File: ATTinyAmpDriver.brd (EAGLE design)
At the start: 30 x 15 mm, 22 parts, among them Q1 BSP100, U1 SPX5205M5-L-3-3, U2 ATTINY5-TSHR, U3 MCP6001, X1 DIODES, X2 INPUT

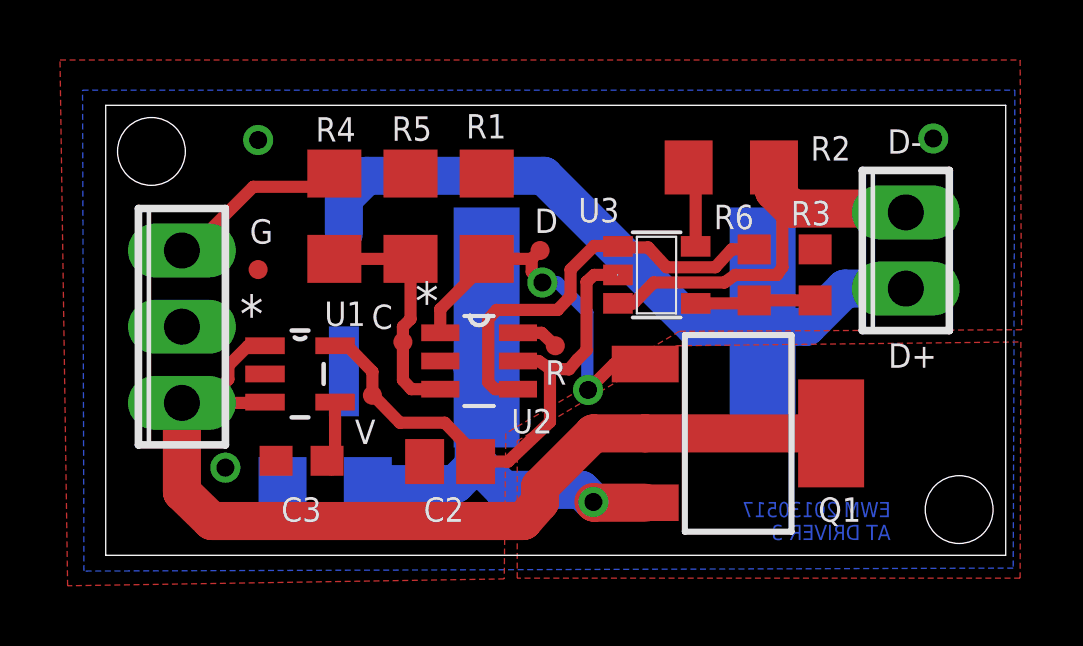
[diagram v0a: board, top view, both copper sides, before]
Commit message: P Channel MOSFET
Changed from Incorrect N-Channel to P-Channel High side switch on the
Driver Circuit.
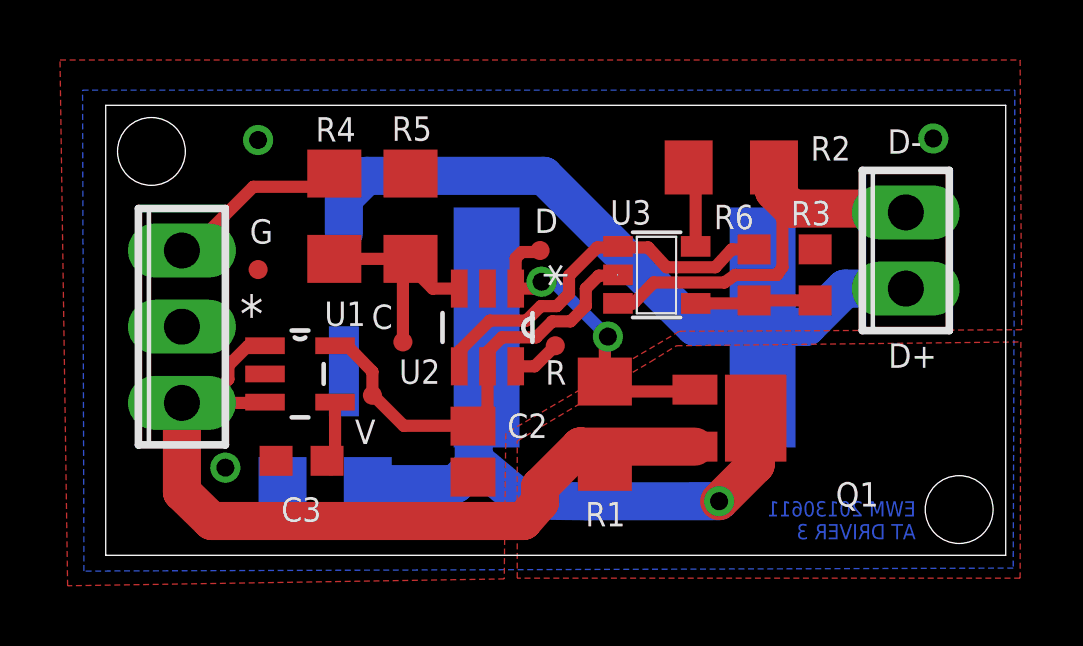
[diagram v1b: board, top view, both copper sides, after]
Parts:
- Q1: value BSP100 -> SI2301CDS; device Personal:SOT223 -> Combined:SOT-23_POWER
- moved R1 7.97 mm to (16.6, 4.37), turned to 90 degrees
- moved U2 1.15 mm to (12.7, 7.59), turned to 270 degrees
- moved C2 0.83 mm to (12.2, 3.45), turned to 270 degrees
- moved Q1 0.77 mm to (21.7, 4.57)
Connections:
- net +14V: now also Q1.P$2, R1.1; no longer Q1.2, Q1.TAB
- net GND: no longer R1.1
- net L+: now also Q1.P$3; no longer Q1.3
- net MOSFET: now also Q1.P$1; no longer Q1.1
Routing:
- net L+: track 15.2 -> 20.8 mm
- net +14V: track 32.4 -> 27.7 mm
- net VCC: track 17.7 -> 14.6 mm
- net MOSFET: track 12.7 -> 10.6 mm
- net MEASURE: track 14.2 -> 12.7 mm
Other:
- board text added: "EWM 20130611 AT DRIVER 3"
- board text removed: "EWM 20130517 AT DRIVER 3"

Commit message: Added Driving transistor for P-FET
Added driver transistor to P Channel MOSFET and capacitor to op-amp
output.
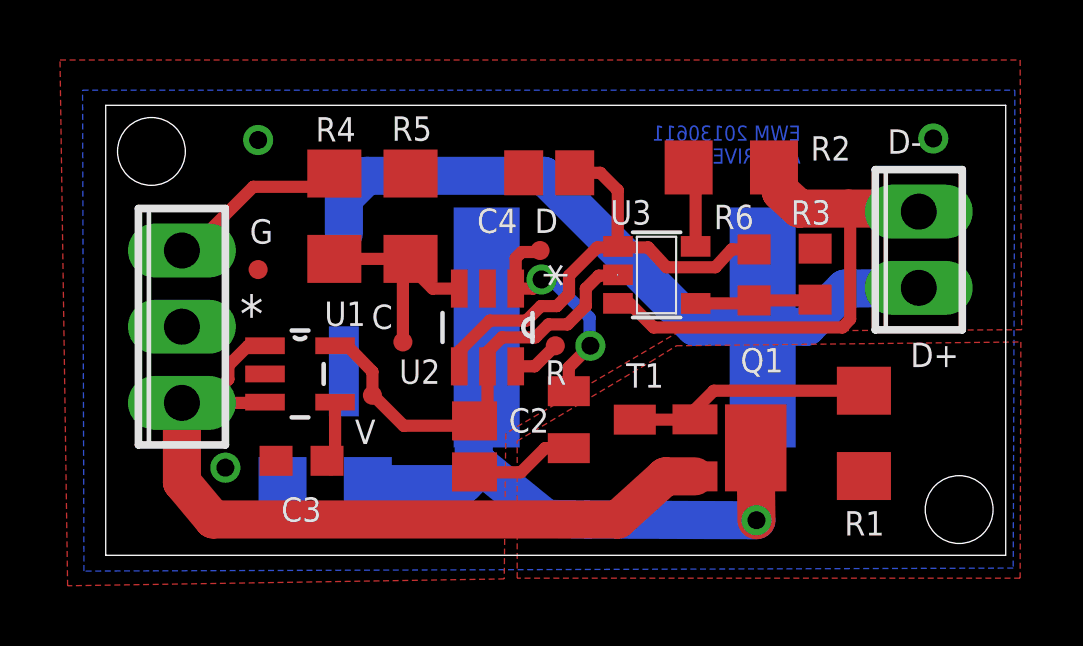
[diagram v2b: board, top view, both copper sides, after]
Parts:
- added C4: .1u, resistor:C0805
- added T1: BC846, transistor-neu-to92:SOT23
- moved R1 8.64 mm to (25.3, 4.06)
- moved Q1 0.99 mm to (21.7, 3.58)
- moved X1 0.43 mm to (27.1, 10.2)
- moved C2 0.18 mm to (12.3, 3.63)
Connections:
- new net N$5: Q1.P$1, R1.2, T1.3
- net GND: now also C4.2, T1.2
- net MEASURE: now also C4.1
- net MOSFET: now also T1.1; no longer Q1.P$1, R1.2
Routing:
- net N$5: track 0.00 -> 8.23 mm
- net MEASURE: track 12.7 -> 16.3 mm
- net GND: track 2.73 -> 6.21 mm
- net MOSFET: track 10.6 -> 7.83 mm
- net D-: track 14.9 -> 17.6 mm
- net +14V: track 27.7 -> 26.7 mm
- net L+: track 20.8 -> 21.5 mm

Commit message: Removed LED filter circuit
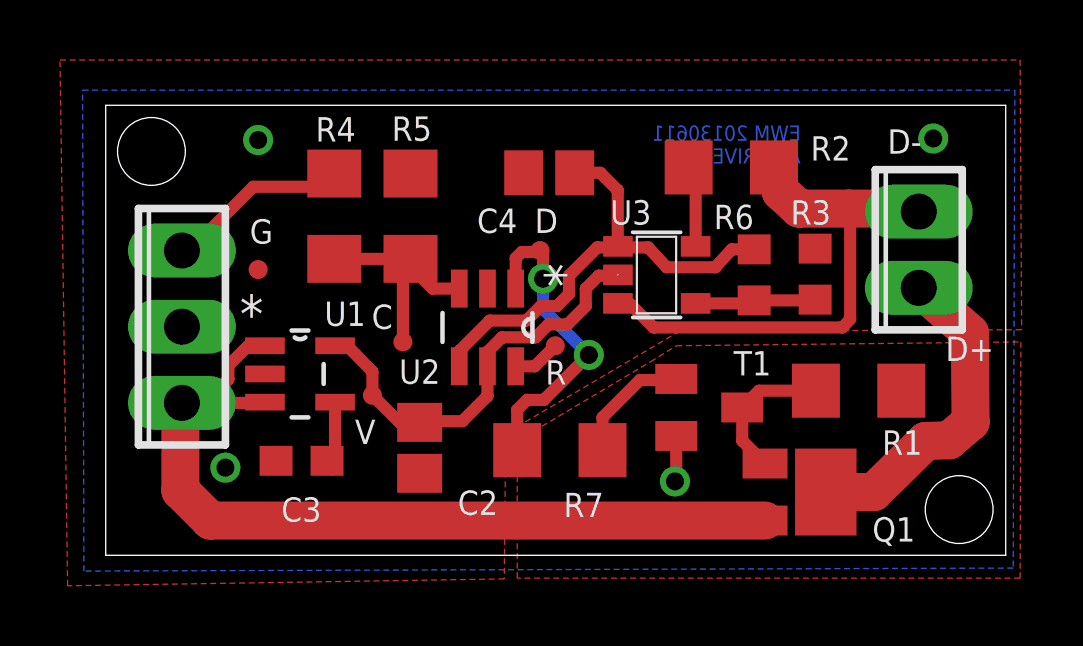
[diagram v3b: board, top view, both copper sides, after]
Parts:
- removed C1: 100u, Personal:CDE-AVE-X
- removed D1: CD1206-B260, Personal:D1206
- removed L1: SRN8040, Personal:SRN8040
- added R7: 10k, resistor:R1206
- R1: value 10k -> 1k
- moved T1 3.60 mm to (20.1, 4.93)
- moved Q1 2.76 mm to (24.0, 2.11)
- moved C2 1.83 mm to (10.5, 3.58)
- moved R1 1.43 mm to (25.1, 5.49), turned to 180 degrees
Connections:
- removed net L+: D1.1, L1.P$1, Q1.P$3
- new net N$6: R7.2, T1.1
- net GND: no longer C1.C-, D1.2
- net MOSFET: now also R7.1; no longer T1.1
- net N$3: now also Q1.P$3; no longer C1.C+, L1.P$2
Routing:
- net L+: track 21.5 -> 0.00 mm, vias 1 -> 0
- net N$3: track 23.3 -> 11.0 mm
- net N$6: track 0.00 -> 4.08 mm
- net N$5: track 8.23 -> 4.87 mm
- net MOSFET: track 7.83 -> 10.6 mm
- net +14V: track 26.7 -> 28.7 mm
- net GND: track 6.21 -> 4.27 mm, vias 3 -> 4

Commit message: Removed Cap from OpAmp Output
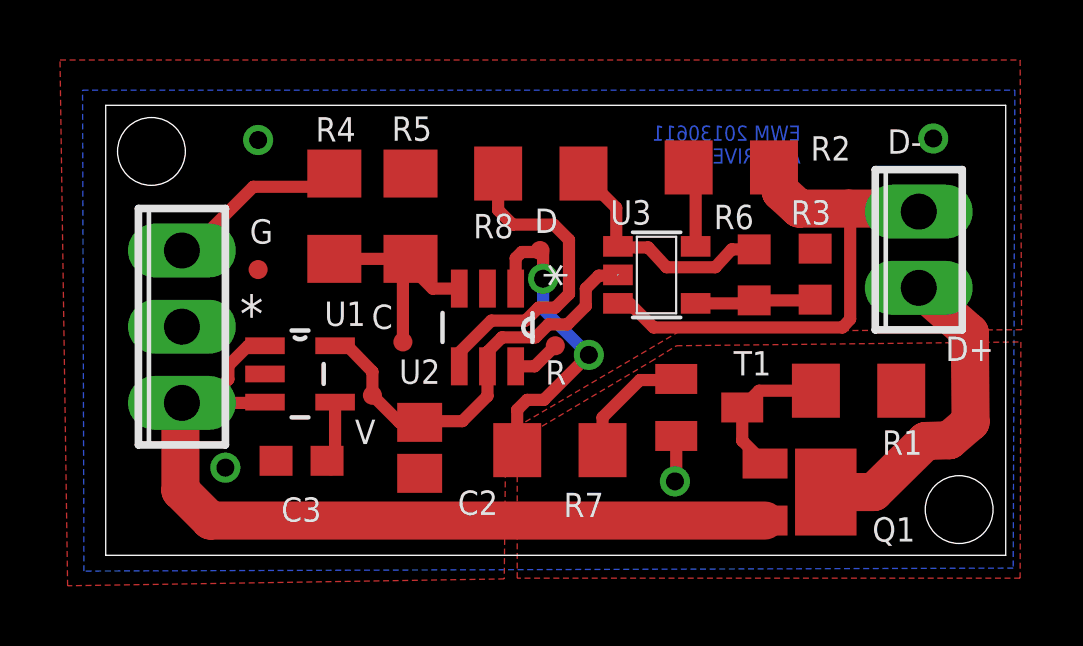
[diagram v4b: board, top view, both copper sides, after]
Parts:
- removed C4: .1u, resistor:C0805
- added R8: 10k, resistor:R1206
- R4: value 910 -> 3.2k
- R5: value 300 -> 1k
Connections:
- new net OPAMP_OUT: R6.1, R8.1, U3.1
- net GND: no longer C4.2
- net MEASURE: now also R8.2; no longer C4.1, R6.1, U3.1
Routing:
- net OPAMP_OUT: track 0.00 -> 8.02 mm
- net MEASURE: track 16.3 -> 10.7 mm
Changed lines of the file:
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@@
 <attribute name="DIGIKEY_COST" value=".69" x="12.7254" y="7.5946" size="1.778" layer="27" rot="R270" display="off"/>
 </element>
-<element name="R4" library="resistor" package="R1206" value="910" x="7.62" y="11.303" smashed="yes" rot="R90">
+<element name="R4" library="resistor" package="R1206" value="3.2k" x="7.62" y="11.303" smashed="yes" rot="R90">
 <attribute name="NAME" x="8.3312" y="14.605" size="0.8128" layer="25" rot="R180"/>
 <attribute name="VALUE" x="10.033" y="9.906" size="1.27" layer="27" rot="R90"/>
@@
 <attribute name="DIGIKEY_COST" value=".05" x="7.62" y="11.303" size="1.778" layer="27" rot="R90" display="off"/>
 </element>
-<element name="R5" library="resistor" package="R1206" value="300" x="10.16" y="11.303" smashed="yes" rot="R90">
+<element name="R5" library="resistor" package="R1206" value="1k" x="10.16" y="11.303" smashed="yes" rot="R90">
 <attribute name="NAME" x="10.8712" y="14.6304" size="0.8128" layer="25" rot="R180"/>
 <attribute name="VALUE" x="12.573" y="9.906" size="1.27" layer="27" rot="R90"/>
@@
 <attribute name="VALUE" x="16.9418" y="6.8326" size="1.27" layer="27" rot="R270"/>
 </element>
-<element name="C4" library="resistor" package="C0805" value=".1u" x="14.7828" y="12.7508" smashed="yes" rot="R180">
-<attribute name="DIGIKEY_COST" value=".10" x="14.7828" y="12.7508" size="1.778" layer="27" rot="R180" display="off"/>
-<attribute name="DIGIKEY" value="445-7534-1-ND" x="14.7828" y="12.7508" size="1.778" layer="27" rot="R180" display="off"/>
-<attribute name="NAME" x="13.716" y="11.557" size="0.8128" layer="25" rot="R180"/>
-<attribute name="VALUE" x="15.6718" y="15.0368" size="1.27" layer="27" rot="R180"/>
-</element>
 <element name="R7" library="resistor" package="R1206" value="10k" x="15.1384" y="3.5052" smashed="yes">
 <attribute name="DIGIKEY_COST" value=".05" x="15.1384" y="3.5052" size="1.778" layer="27" display="off"/>
@@
 <attribute name="NAME" x="15.2654" y="1.27" size="0.8128" layer="25"/>
 <attribute name="VALUE" x="13.7414" y="1.0922" size="1.27" layer="27"/>
+</element>
+<element name="R8" library="resistor" package="R1206" value="10k" x="14.5034" y="12.7254" smashed="yes" rot="R180">
+<attribute name="DIGIKEY_COST" value=".05" x="14.5034" y="12.7254" size="1.778" layer="27" rot="R180" display="off"/>
+<attribute name="DIGIKEY" value="RMCF1206JT10K0CT-ND" x="14.5034" y="12.7254" size="1.778" layer="27" rot="R180" display="off"/>
+<attribute name="NAME" x="13.589" y="11.3792" size="0.8128" layer="25" rot="R180"/>
+<attribute name="VALUE" x="15.9004" y="15.1384" size="1.27" layer="27" rot="R180"/>
 </element>
 </elements>
@@
 <wire x1="19.6642" y1="12.6958" x2="19.4314" y2="12.9286" width="0.4064" layer="1"/>
 <contactref element="T1" pad="2"/>
-<contactref element="C4" pad="2"/>
 <via x="18.9738" y="2.4638" extent="1-16" drill="0.6"/>
 <wire x1="19.0168" y1="3.9776" x2="19.0168" y2="2.4814" width="0.4064" layer="1"/>
@@
 <signal name="MEASURE">
 <contactref element="U2" pad="4"/>
-<contactref element="U3" pad="1"/>
-<contactref element="R6" pad="1"/>
-<wire x1="21.6154" y1="10.1972" x2="20.8652" y2="10.1972" width="0.4064" layer="1"/>
-<wire x1="20.8652" y1="10.1972" x2="20.32" y2="9.6012" width="0.4064" layer="1"/>
-<wire x1="20.32" y1="9.6012" x2="18.6944" y2="9.6012" width="0.4064" layer="1"/>
-<wire x1="18.6944" y1="9.6012" x2="18.0848" y2="10.2616" width="0.4064" layer="1"/>
-<wire x1="18.0848" y1="10.2616" x2="17.1098" y2="10.2616" width="0.4064" layer="1"/>
-<wire x1="17.1098" y1="10.2616" x2="17.0742" y2="10.2972" width="0.4064" layer="1"/>
-<wire x1="11.7856" y1="6.2992" x2="11.7856" y2="6.8072" width="0.4064" layer="1"/>
-<wire x1="11.7856" y1="6.8072" x2="12.8016" y2="7.8232" width="0.4064" layer="1"/>
-<wire x1="12.8016" y1="7.8232" x2="14.0208" y2="7.8232" width="0.4064" layer="1"/>
-<wire x1="14.0208" y1="7.8232" x2="14.5034" y2="8.3058" width="0.4064" layer="1"/>
-<wire x1="14.5034" y1="8.3058" x2="15.0368" y2="8.3058" width="0.4064" layer="1"/>
-<wire x1="15.0368" y1="8.3058" x2="15.4432" y2="8.7122" width="0.4064" layer="1"/>
-<wire x1="15.4432" y1="8.7122" x2="15.4432" y2="9.3218" width="0.4064" layer="1"/>
-<wire x1="15.4432" y1="9.3218" x2="16.383" y2="10.2616" width="0.4064" layer="1"/>
-<wire x1="16.383" y1="10.2616" x2="17.0386" y2="10.2616" width="0.4064" layer="1"/>
-<wire x1="17.0386" y1="10.2616" x2="17.0742" y2="10.2972" width="0.4064" layer="1"/>
-<contactref element="C4" pad="1"/>
-<wire x1="15.6328" y1="12.7508" x2="16.4846" y2="12.7508" width="0.4064" layer="1"/>
-<wire x1="16.4846" y1="12.7508" x2="17.0688" y2="12.1666" width="0.4064" layer="1"/>
-<wire x1="17.0688" y1="12.1666" x2="17.0688" y2="10.3026" width="0.4064" layer="1"/>
-<wire x1="17.0688" y1="10.3026" x2="17.0742" y2="10.2972" width="0.4064" layer="1"/>
+<contactref element="R8" pad="2"/>
+<wire x1="11.7856" y1="6.2992" x2="11.7856" y2="6.7564" width="0.4064" layer="1"/>
+<wire x1="11.7856" y1="6.7564" x2="12.8524" y2="7.8232" width="0.4064" layer="1"/>
+<wire x1="12.8524" y1="7.8232" x2="13.9954" y2="7.8232" width="0.4064" layer="1"/>
+<wire x1="13.9954" y1="7.8232" x2="14.4272" y2="8.255" width="0.4064" layer="1"/>
+<wire x1="14.4272" y1="8.255" x2="14.986" y2="8.255" width="0.4064" layer="1"/>
+<wire x1="14.986" y1="8.255" x2="15.4432" y2="8.7122" width="0.4064" layer="1"/>
+<wire x1="15.4432" y1="8.7122" x2="15.4432" y2="10.5156" width="0.4064" layer="1"/>
+<wire x1="15.4432" y1="10.5156" x2="14.9352" y2="11.0236" width="0.4064" layer="1"/>
+<wire x1="14.9352" y1="11.0236" x2="13.5636" y2="11.0236" width="0.4064" layer="1"/>
+<wire x1="13.5636" y1="11.0236" x2="13.081" y2="11.5062" width="0.4064" layer="1"/>
+<wire x1="13.081" y1="11.5062" x2="13.081" y2="12.725" width="0.4064" layer="1"/>
+<wire x1="13.081" y1="12.725" x2="13.0814" y2="12.7254" width="0.4064" layer="1"/>
 </signal>
 <signal name="MOSFET">
@@
 <wire x1="18.9812" y1="5.842" x2="19.0168" y2="5.8776" width="0.4064" layer="1"/>
 </signal>
+<signal name="OPAMP_OUT">
+<contactref element="U3" pad="1"/>
+<contactref element="R6" pad="1"/>
+<contactref element="R8" pad="1"/>
+<wire x1="21.6154" y1="10.1972" x2="20.8652" y2="10.1972" width="0.4064" layer="1"/>
+<wire x1="20.8652" y1="10.1972" x2="20.32" y2="9.6012" width="0.4064" layer="1"/>
+<wire x1="20.32" y1="9.6012" x2="18.6944" y2="9.6012" width="0.4064" layer="1"/>
+<wire x1="18.6944" y1="9.6012" x2="18.0848" y2="10.2616" width="0.4064" layer="1"/>
+<wire x1="18.0848" y1="10.2616" x2="17.1098" y2="10.2616" width="0.4064" layer="1"/>
+<wire x1="17.1098" y1="10.2616" x2="17.0742" y2="10.2972" width="0.4064" layer="1"/>
+<wire x1="17.0688" y1="10.3026" x2="17.0742" y2="10.2972" width="0.4064" layer="1"/>
+<wire x1="15.9254" y1="12.7254" x2="15.9254" y2="12.675" width="0.4064" layer="1"/>
+<wire x1="15.9254" y1="12.675" x2="17.018" y2="11.5824" width="0.4064" layer="1"/>
+<wire x1="17.018" y1="11.5824" x2="17.018" y2="10.3534" width="0.4064" layer="1"/>
+<wire x1="17.018" y1="10.3534" x2="17.0742" y2="10.2972" width="0.4064" layer="1"/>
+</signal>
 </signals>

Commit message: Low Pass filter before OpAmp
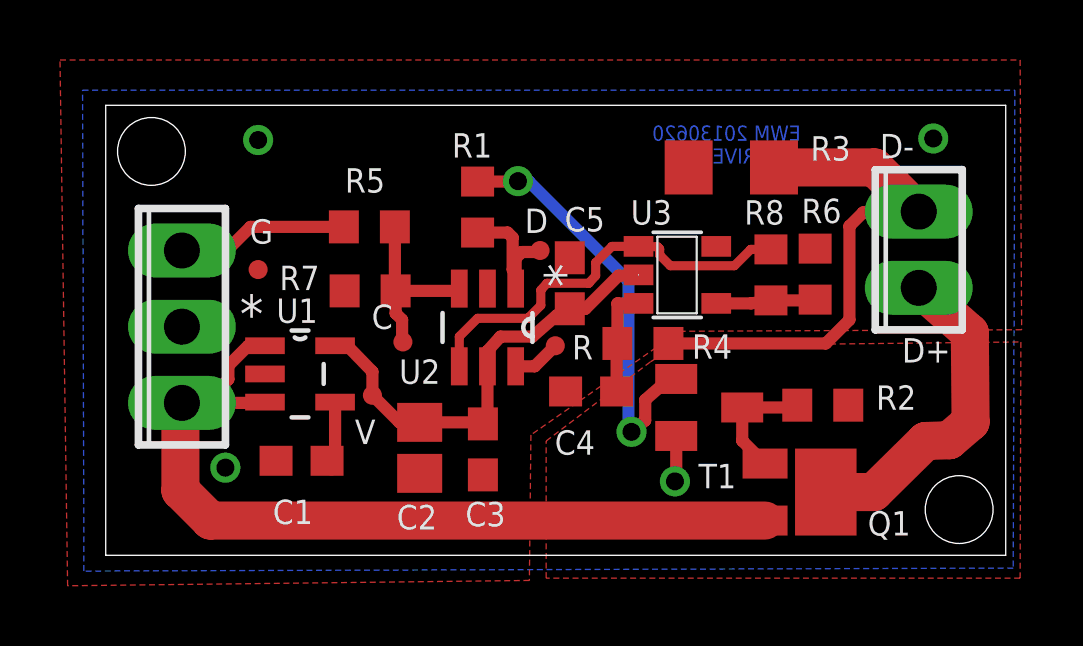
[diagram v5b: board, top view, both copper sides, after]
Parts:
- added C1: 10n, resistor:C0603
- added C4, C5: .1u, resistor:C0603
- C2: value .1u -> 10u
- C3: value 10n -> .1u
- R1: value 1k -> 10k; device resistor:R1206 -> resistor:R0603
- R2: value .1 -> 1k; device resistor:R1206 -> resistor:R0603
- R3: value 1K -> .1; device resistor:R0603 -> resistor:R1206
- R4: value 3.2k -> 10k; device resistor:R1206 -> resistor:R0603
- R5: value 1k -> 3.2k; device resistor:R1206 -> resistor:R0603
- R6: value 28.7K -> 1K
- R7: value 10k -> 1k; device resistor:R1206 -> resistor:R0603
- R8: value 10k -> 28.7K; device resistor:R1206 -> resistor:R0603
- moved R1 14.1 mm to (12.4, 11.6), turned to 90 degrees
- moved R4 11.1 mm to (17.9, 7.06), turned to 180 degrees
- moved R2 8.49 mm to (23.9, 5.00), turned to 180 degrees
- moved R8 8.38 mm to (22.2, 9.35), turned to 270 degrees
- moved R7 8.26 mm to (8.81, 8.81), turned to 180 degrees
- moved C3 6.06 mm to (12.6, 3.53), turned to 270 degrees
- moved R3 4.52 mm to (20.9, 12.9), turned to 0 degrees
- moved R6 2.03 mm to (23.6, 9.37)
- moved R5 1.42 mm to (8.79, 10.9), turned to 180 degrees
- moved U3 0.69 mm to (19.1, 9.35)
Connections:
- removed net OPAMP_OUT: R6.1, R8.1, U3.1
- new net N$7: C4.1, R4.2, U3.3
- net +14V: now also R2.1; no longer R1.1
- net BLINK: now also R7.1; no longer R4.1
- net D-: now also R3.2, R4.1; no longer R2.2, U3.3
- net GND: now also C1.2, C4.2, C5.2, R6.1, R7.2; no longer R2.1, R5.2
- net MEASURE: now also R8.1, U3.1; no longer R8.2
- net MOSFET: now also R1.1; no longer R7.1
- net N$1: now also R5.2; no longer R4.2
- net N$2: now also C1.1; no longer C3.1
- net N$4: now also R8.2; no longer R3.2
- net N$5: now also R2.2; no longer R1.2
- net N$6: now also R1.2; no longer R7.2
- net VCC: now also C3.1, C5.1
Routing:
- net N$6: track 4.08 -> 14.1 mm, vias 0 -> 2
- net OPAMP_OUT: track 8.02 -> 0.00 mm
- net MOSFET: track 10.6 -> 4.38 mm, vias 2 -> 0
- net N$7: track 0.00 -> 3.67 mm
- net MEASURE: track 10.7 -> 13.8 mm
- net GND: track 4.27 -> 1.54 mm
- net BLINK: track 7.60 -> 6.10 mm
- net VCC: track 14.3 -> 15.3 mm
- net N$5: track 4.87 -> 4.05 mm
- net N$4: track 4.04 -> 3.32 mm
- net N$1: track 6.40 -> 5.72 mm
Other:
- board text added: "EWM 20130620 AT DRIVER 3"
- board text removed: "EWM 20130611 AT DRIVER 3"
